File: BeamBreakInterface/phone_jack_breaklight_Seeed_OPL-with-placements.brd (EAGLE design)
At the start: 31.8 x 13.3 mm, 10 parts, among them J1 ST-PJ-312, J2 4P-SMD-2.0-90D, Q1 BSS138W-7-F

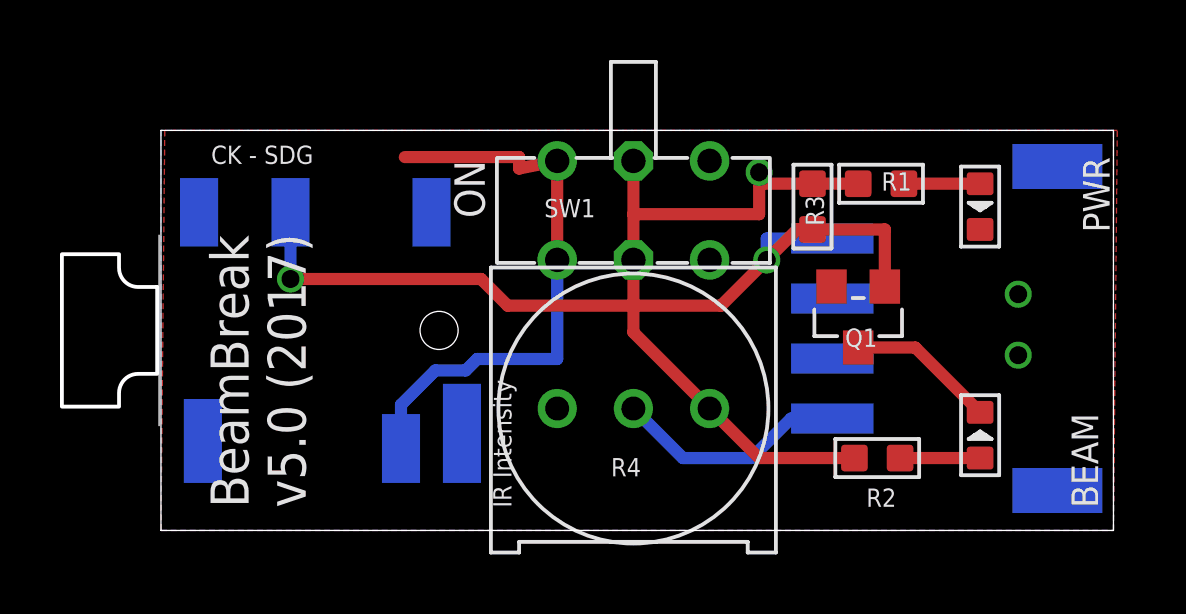
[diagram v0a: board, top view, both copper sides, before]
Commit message: Updated design to fix error
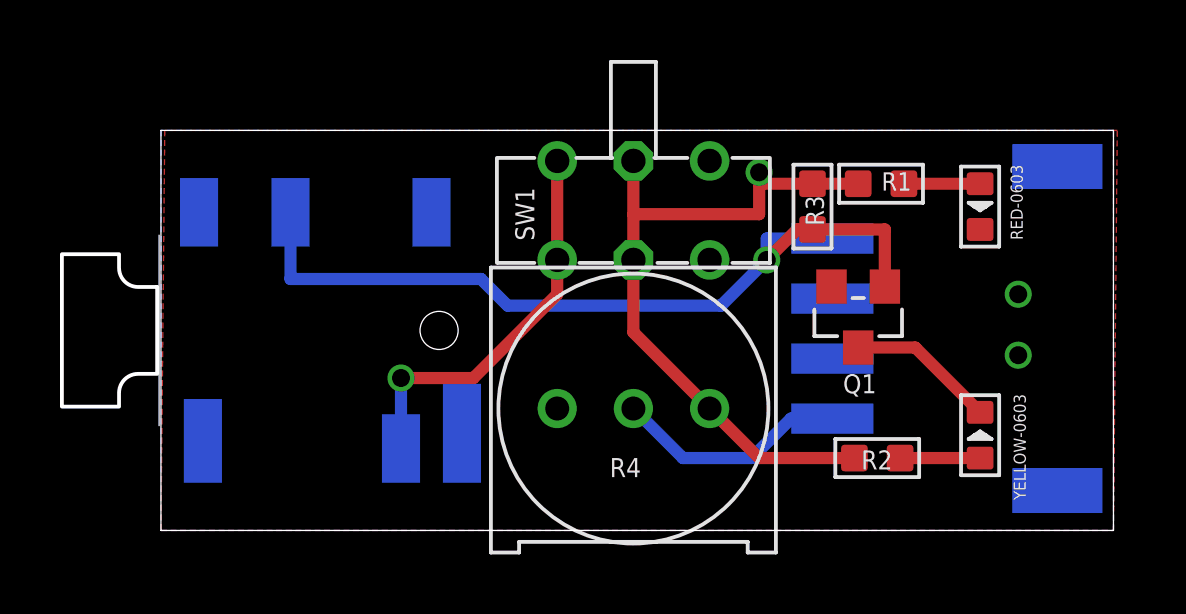
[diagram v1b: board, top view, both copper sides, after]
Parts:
- RED-0603: value RED-0603 -> PWR
- YELLOW-0603: value YELLOW-0603 -> BEAM
- renumbered BEAM to YELLOW-0603, PWR to RED-0603
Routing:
- net N$2: track 19.4 -> 13.2 mm, vias 0 -> 1
- net SIG: vias 2 -> 1
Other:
- board text added: "BeamBreak v5.1 (2017)"
- board text removed: "BeamBreak v5.0 (2017)"
